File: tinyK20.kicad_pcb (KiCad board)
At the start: 2 copper layers, 45.8 x 73.7 mm, 78 parts, among them CON1 USB-MINI-B, P1 CONN_1, P10 CONN_1, P11 CONN_1, P12 CONN_1, P13 CONN_1, P14 CONN_1, P15 CONN_1, P16 CONN_1, P17 CONN_1, P18 CONN_1, P19 CONN_1, P2 CONN_1, P20 CONN_1, P21 CONN_1, P22 CONN_1, P23 CONN_1, P24 CONN_1, P25 CONN_1, P26 CONN_1, P27 CONN_1, P28 CONN_1, P29 CONN_1, P3 CONN_1, P30 CONN_1, P31 CONN_1, P32 CONN_1, P33 CONN_1, P34 CONN_1, P35 CONN_5X2, P36 CONN_1, P37 CONN_1, P38 CONN_5X2, P4 CONN_1, P41 CONN_1, P5 CONN_1, P6 CONN_1, P7 CONN_1, P8 CONN_1, P9 CONN_1, SW1 SW_PUSH, U1 MK20DX128VFT5, U2 LT1129CST-3.3, U3 74LS126, X3 MOLEX-MICRO-SD, Y1 Crystal, Y2 Crystal_Small

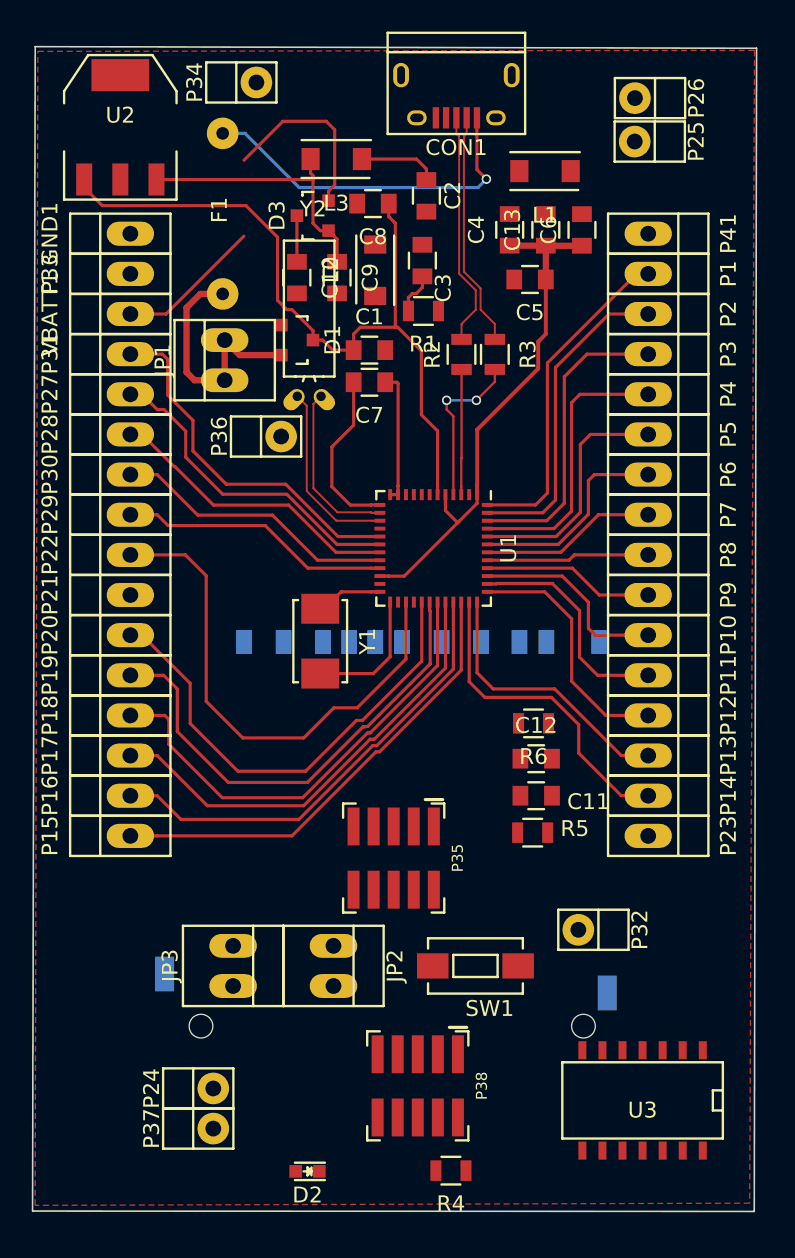
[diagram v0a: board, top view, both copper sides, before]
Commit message: complete pin connections
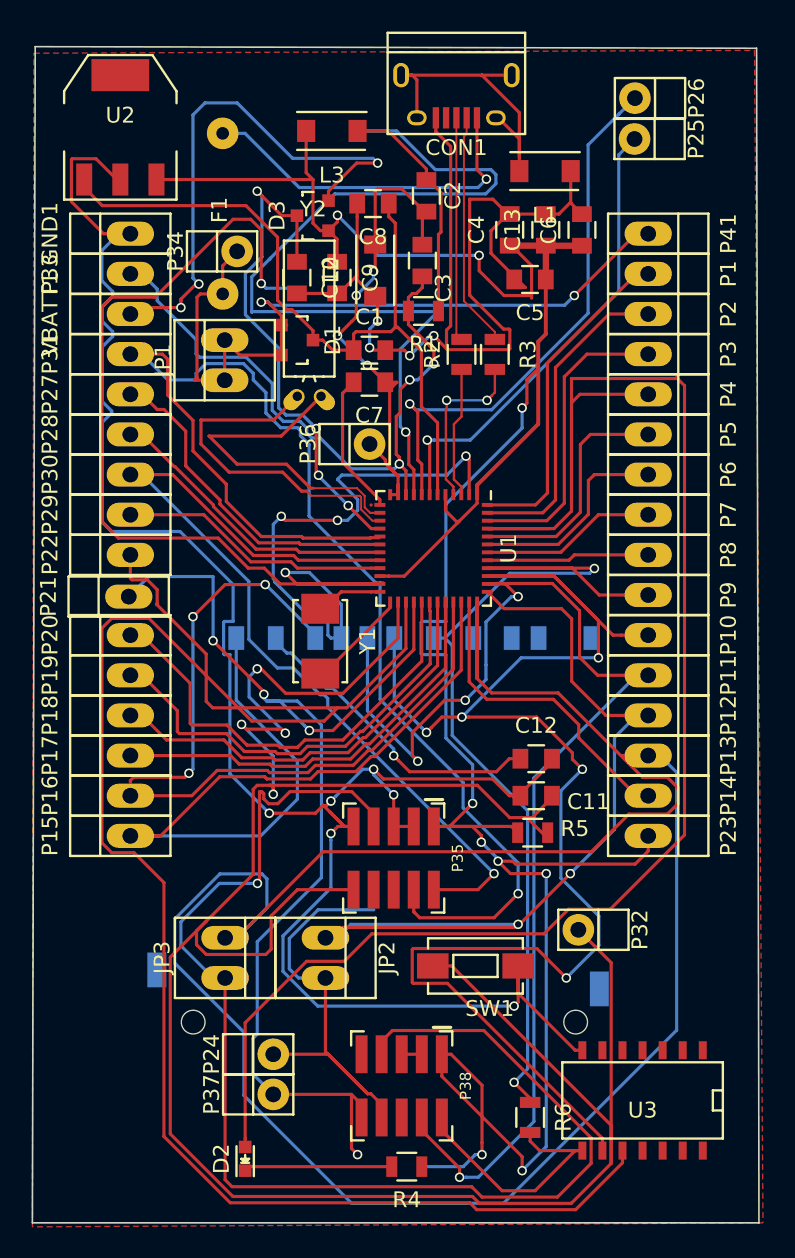
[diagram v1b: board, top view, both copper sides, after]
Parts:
- moved R6 24.9 mm to (81.8, 112.2), turned to 270 degrees
- moved P34 10.8 mm to (63.2, 58.7)
- moved P36 5.62 mm to (71.6, 70.9)
- moved P24 4.37 mm to (65.5, 109.5)
- moved P37 4.37 mm to (65.5, 112.0)
- moved D2 4.02 mm to (63.8, 114.8), turned to 90 degrees
- moved R4 2.81 mm to (74.0, 115.3)
- moved L3 1.80 mm to (69.2, 49.8)
- moved P38 1.02 mm to (73.7, 110.2)
- moved JP2 0.72 mm to (68.8, 102.1)
- moved JP3 0.72 mm to (62.5, 102.1)
- moved X3 0.56 mm to (72.6, 81.9)
- moved P25 0.16 mm to (88.4, 49.0)
- moved P21 0.14 mm to (55.8, 74.2)
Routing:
- net GND: track 0.00 -> 287.6 mm, vias 0 -> 15
- net RESET: track 0.00 -> 153.4 mm, vias 0 -> 4
- net 3V3: track 50.4 -> 178.7 mm, vias 0 -> 9
- net Net-(JP3-Pad1): track 17.5 -> 142.6 mm
- net LED: track 17.7 -> 106.3 mm
- net PTC6: track 12.7 -> 96.3 mm, vias 0 -> 5
- net PTB0: track 32.6 -> 114.9 mm
- net UART1_RX: track 0.00 -> 82.3 mm, vias 0 -> 1
- net PTB1: track 0.00 -> 71.7 mm, vias 0 -> 4
- net PTC5: track 14.3 -> 82.8 mm, vias 0 -> 4
- net Net-(C2-Pad1): track 5.04 -> 70.4 mm, vias 0 -> 1
- net SWD_CLK: track 23.0 -> 82.7 mm, vias 0 -> 1
- net PTC7: track 10.9 -> 62.0 mm, vias 0 -> 2
- net Net-(JP2-Pad1): track 15.7 -> 58.6 mm, vias 0 -> 2
- net SWD_IO: track 18.0 -> 58.2 mm, vias 0 -> 1
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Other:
- board size 45.8 x 73.7 mm -> 46 x 74.4 mm
- net class Default: trace_width 0.4 -> 0.2

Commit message: update pcb
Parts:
- added C14: 22nF, Capacitors_SMD:C_0805, F.Cu at (62.0, 76.5)
- added C15: 22nF, Capacitors_SMD:C_0805, F.Cu at (62.7, 80.5)
- added R7: 1M, Capacitors_SMD:C_0402, F.Cu at (64.5, 78.5)
- U4: renamed from X3; value MOLEX-MICRO-SD -> 105027-0001; footprint Connect:SD_Card_Receptacle -> sd-socket:105027-0001
- moved R4 4.83 mm to (69.2, 115.3)
- moved Y1 2.57 mm to (68.3, 79.5)
- moved U4 0.87 mm to (73.4, 82.0)
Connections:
- CON1 pad 4: (no net) -> Net-(CON1-Pad4)
- P35 pad 6: (no net) -> Net-(P35-Pad6)
- P38 pad 6: (no net) -> Net-(P38-Pad6)
- P38 pad 9: (no net) -> Net-(P38-Pad9)
- U3 pad 14: (no net) -> VCC
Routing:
- net GND: track 287.6 -> 175.4 mm, vias 15 -> 11
- net Net-(JP3-Pad1): track 142.6 -> 50.1 mm, vias 0 -> 2
- net Net-(C2-Pad1): track 70.4 -> 28.2 mm, vias 1 -> 2
- net LED: track 106.3 -> 83.7 mm, vias 0 -> 2
- net PTC0: track 53.4 -> 32.3 mm, vias 3 -> 1
- net PTB0: track 114.9 -> 95.5 mm, vias 0 -> 2
- net SWD_CLK: track 82.7 -> 63.5 mm, vias 1 -> 3
- net PTC1: track 53.0 -> 37.6 mm, vias 0 -> 1
- net PTC6: track 96.3 -> 84.8 mm
- net /xtal_P: track 22.1 -> 12.2 mm
- net /xtal_N: track 22.0 -> 12.3 mm
- net /x+: track 6.51 -> 15.9 mm
- net /x-: track 4.24 -> 13.5 mm
- net +3.3V: track 19.7 -> 13.5 mm
- net Net-(D2-Pad1): track 9.38 -> 4.56 mm
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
